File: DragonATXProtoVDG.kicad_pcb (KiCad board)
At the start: 2 copper layers, 159.4 x 85.5 mm, 68 parts, among them IC1 74LS273, IC2 MC6847, IC3 MC14053, J1 Video Output, J2 Board Interconnect Male, J3 JTAG, Q1 MMBT4401, Q2 NPN, Q3 NPN, Q4 NPN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

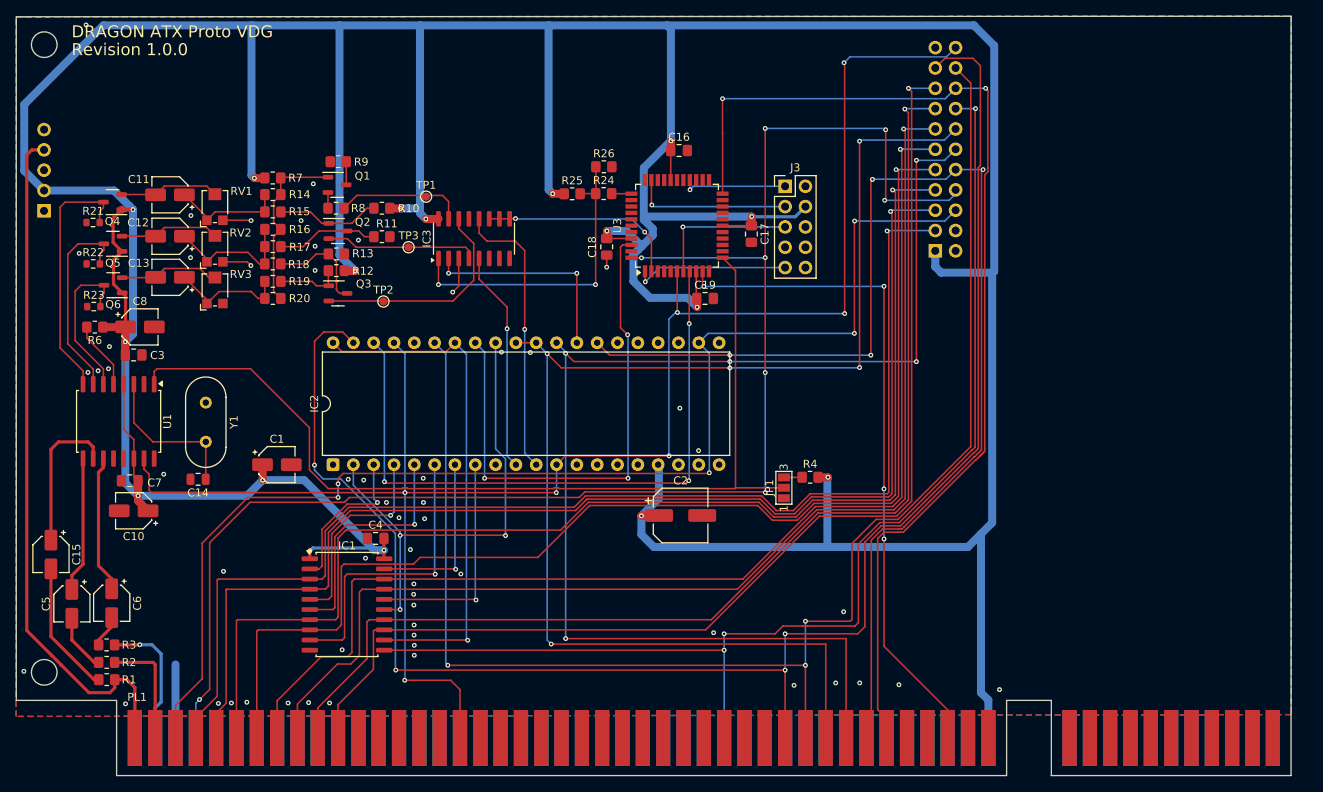
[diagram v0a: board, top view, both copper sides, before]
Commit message: upgrade card edge spec
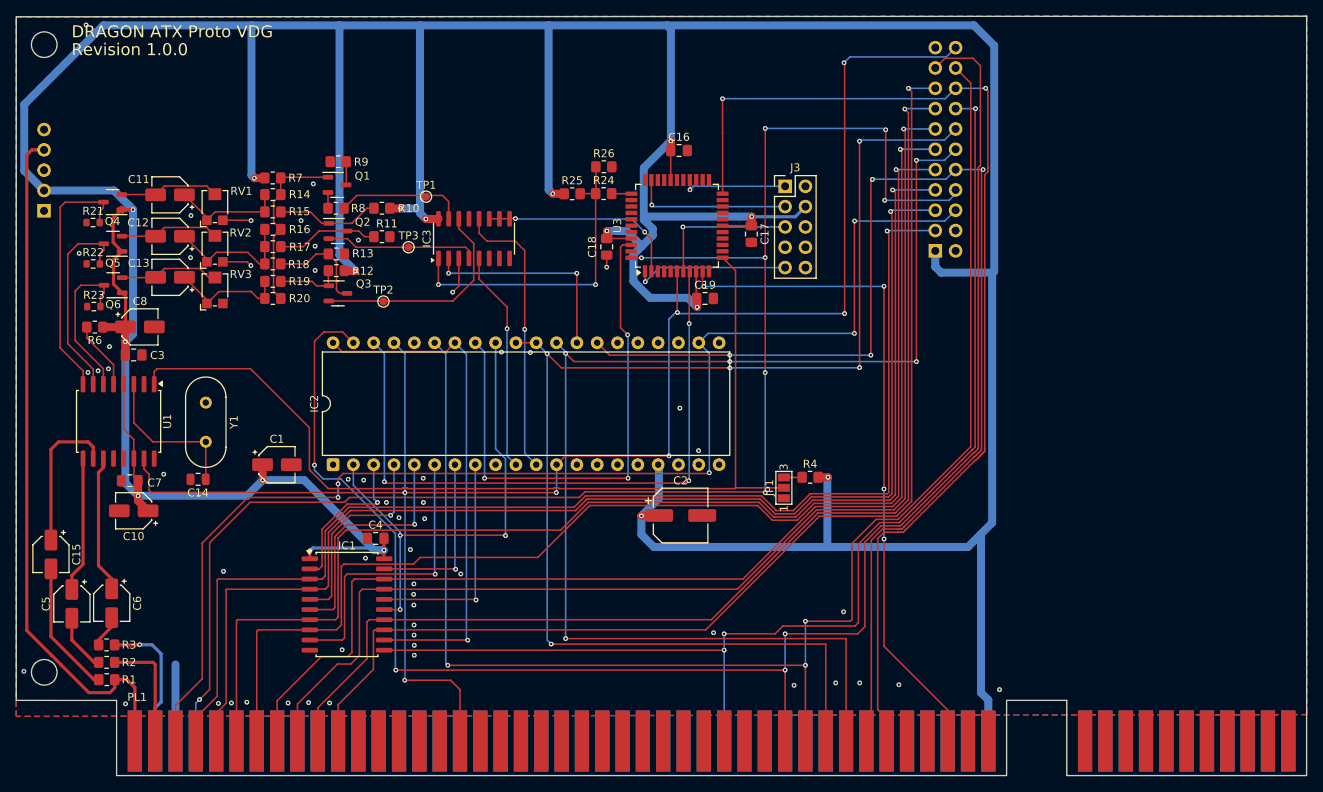
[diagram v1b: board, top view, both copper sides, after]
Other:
- board size 159.4 x 85.5 mm -> 161.3 x 85.5 mm

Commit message: prepare for fabrication
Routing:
- net /HS: track 193.6 -> 180.9 mm, vias 8 -> 6
- net /DL7: track 144.7 -> 143.9 mm, vias 1 -> 0
- net phiB: vias 1 -> 0
- net phiA: vias 1 -> 0
- net GND: vias 56 -> 60

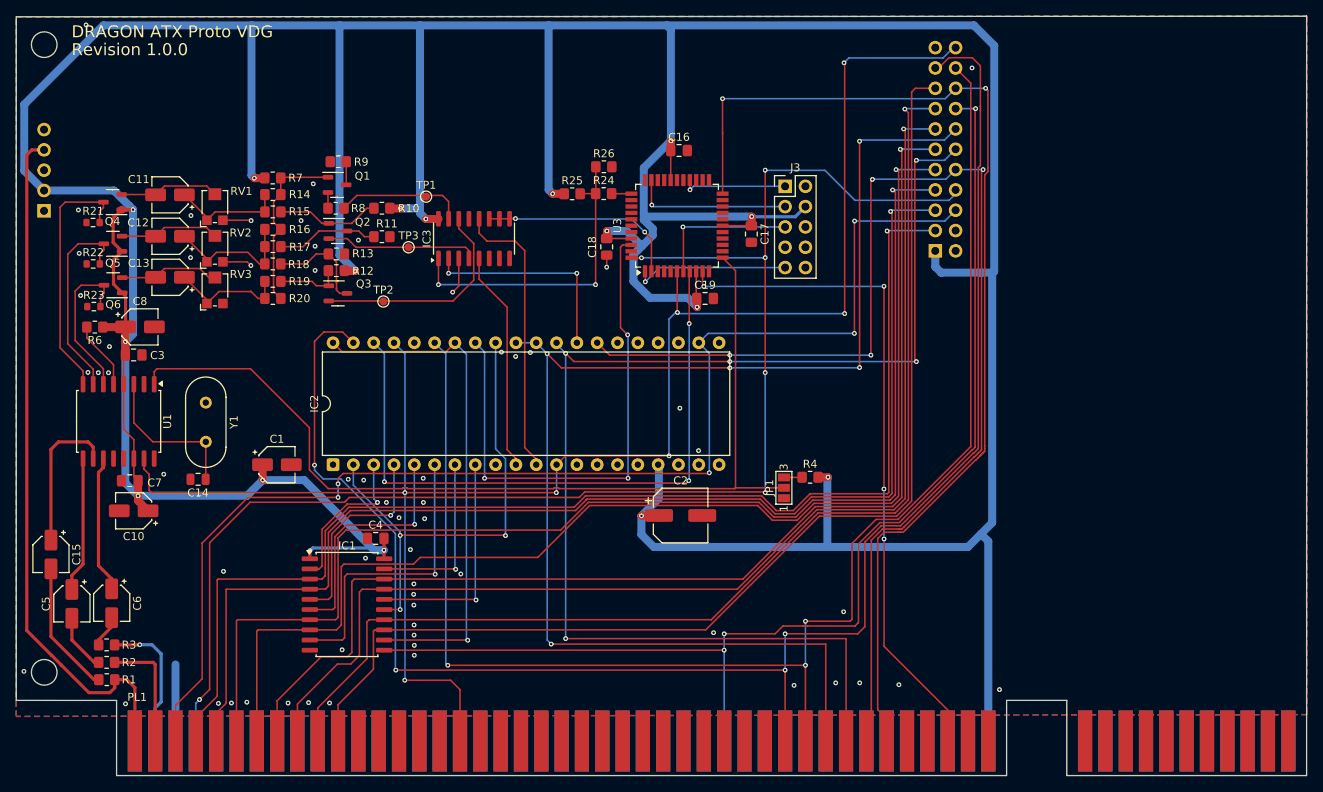
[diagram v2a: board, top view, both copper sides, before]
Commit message: refine design for ATF1504
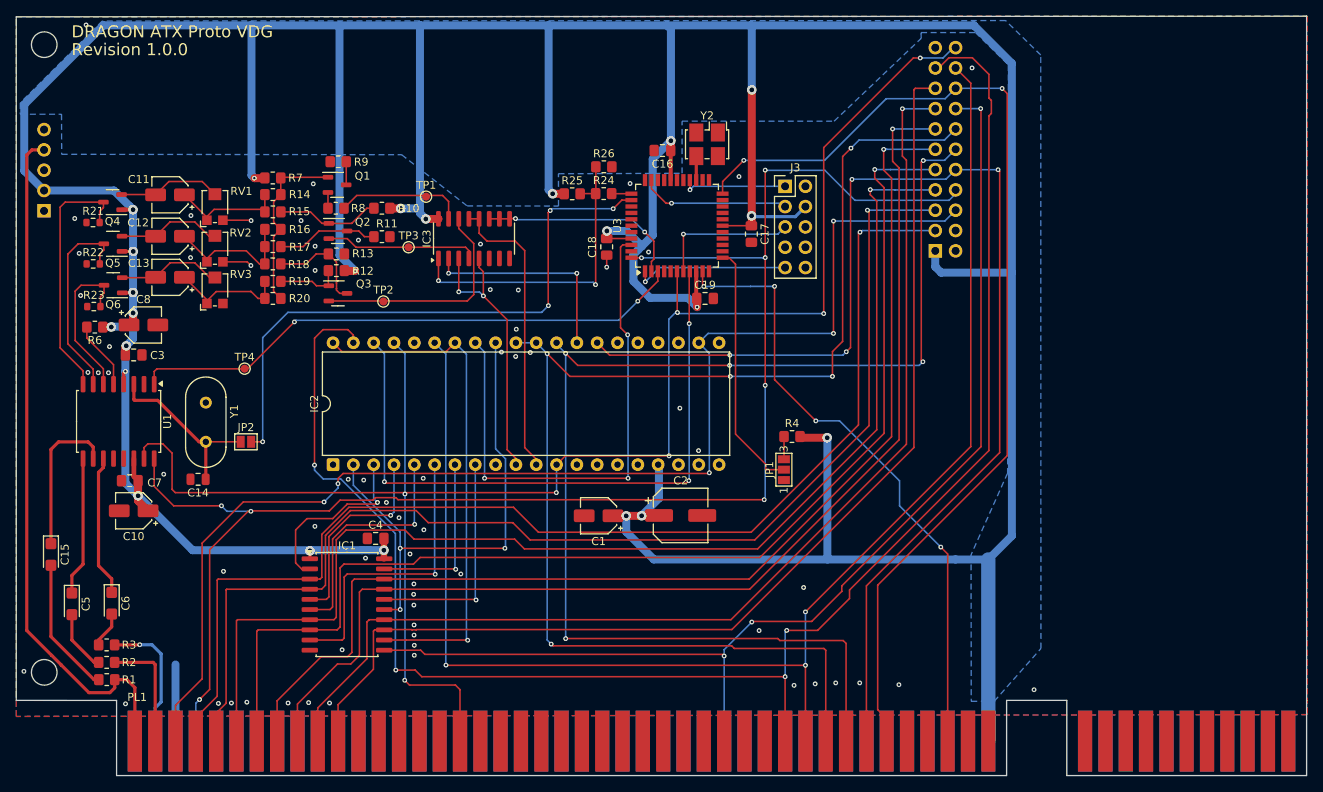
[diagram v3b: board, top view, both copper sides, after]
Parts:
- added JP2: FormatClock, Jumper:SolderJumper-2_P1.3mm_Open_Pad1.0x1.5mm, F.Cu at (92.6, 77.7)
- added TP4: TestPoint_FrameFormat, TestPoint:TestPoint_Pad_D1.0mm, F.Cu at (92.4, 68.6)
- added Y2: 4.433618MHz, Oscillator:Oscillator_SMD_SeikoEpson_SG8002LB-4Pin_5.0x3.2mm_HandSoldering, F.Cu at (150.2, 40.5)
- C15, C5, C6: footprint Capacitor_SMD:CP_Elec_4x5.4 -> Capacitor_Tantalum_SMD:CP_EIA-3216-12_Kemet-S
- U3: value ATF1504ASL-xAx44 -> ATF1502ASL-xAx44
- moved C1 40.7 mm to (136.7, 87.0), turned to 180 degrees
- moved R4 5.57 mm to (160.9, 77.1)
- moved JP1 2.27 mm to (159.8, 81.2)
- moved C16 2.08 mm to (144.7, 41.3), turned to 180 degrees
- moved C8 0.49 mm to (79.8, 63.1)
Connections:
- IC3 pad 13: GND -> phiA
- IC3 pad 3: GND -> phiB
- U1 pad 1: Format -> FrmFormat
- U1 pad 16: ~{NHS} -> /HS
- U3 pad 25: unconnected-(U3-I/O-Pad25) -> PALClock
- U3 pad 3: unconnected-(U3-I/O-Pad3) -> FrmFormat
- U3 pad 30: unconnected-(U3-I/O-Pad30) -> LINE_PULSE
- U3 pad 31: unconnected-(U3-I/O-Pad31) -> SYNC_CONTROL
- U3 pad 33: unconnected-(U3-I/O-Pad33) -> CHROMA_CONTROL
- U3 pad 35: unconnected-(U3-I/O/GCLK3-Pad35) -> FMT_CLOCK
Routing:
- net Format: track 119.4 -> 31.5 mm
- net FMT_CLOCK: track 0.00 -> 74.5 mm, vias 0 -> 4
- net FrmFormat: track 0.00 -> 70.5 mm, vias 0 -> 2
- net /HS: track 180.9 -> 197.8 mm, vias 6 -> 8
- net phiB: track 27.7 -> 35.1 mm, vias 0 -> 2
- net E: track 84.6 -> 78.3 mm
- net /DL3: track 152.7 -> 147.7 mm
- net /RAS: track 147.5 -> 142.8 mm
- net /~{A}/G: track 184.1 -> 179.3 mm
- net GND: track 22.8 -> 18.3 mm, vias 60 -> 67
- net /DL0: track 153.3 -> 148.8 mm
- net /VCLK: track 134.6 -> 130.3 mm
- net /DL6: track 144.3 -> 140.3 mm
- net /DL2: track 154.9 -> 151.1 mm
- net /DL7: track 143.9 -> 140.1 mm
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- added copper zone on B.Cu, net +5V

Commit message: update board render
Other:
- board text added: "JP1 - Format 1-2=PAL 2-3=NTSC JP2 - Clock Source open = direct closed = format controlled"
- board text added: "Revision 1.0.1"
- board text added: "Right pad R14 = Y R15 = B-Y R17 = Y-B R18 = Y-R R19 = R-Y Left Pad R14 & R15 = B-Y+Y R16 & R17 & R18 = Y-B+Y-R+Y R19 & R20 = R-Y+Y"
- board text added: "Test Points TP1 = Luma TP2 = PhiA TP3 = PhiB TP4 = Format Q6/R23 = Red Q5/R22 = Green Q4/R21 = Blue C5 = Chroma C6 = Luma C15 = Composite"
- board text removed: "Revision 1.0.0"
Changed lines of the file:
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@@
 		(layer "User.3")
 	)
-	(gr_text "Revision 1.0.0"
+	(gr_text "Right pad\nR14 = Y\nR15 = B-Y\nR17 = Y-B\nR18 = Y-R\nR19 = R-Y\n\nLeft Pad\nR14 & R15 = B-Y+Y\nR16 & R17 & R18 = Y-B+Y-R+Y\nR19 & R20 = R-Y+Y"
+		(at 194.9958 79.9084 0)
+		(layer "F.SilkS")
+		(effects
+			(font
+				(size 1 1)
+				(thickness 0.1)
+			)
+			(justify left bottom)
+		)
+	)
+	(gr_text "Test Points\n\nTP1 = Luma\nTP2 = PhiA\nTP3 = PhiB\nTP4 = Format\nQ6/R23 = Red\nQ5/R22 = Green\nQ4/R21 = Blue\nC5 = Chroma\nC6 = Luma\nC15 = Composite"
+		(at 194.9958 61.1632 0)
+		(layer "F.SilkS")
+		(effects
+			(font
+				(size 1 1)
+				(thickness 0.1)
+			)
+			(justify left bottom)
+		)
+	)
+	(gr_text "Revision 1.0.1"
 		(at 70.7898 29.5783 0)
 		(layer "F.SilkS")
@@
 			)
 			(justify left bottom)
+		)
+	)
+	(gr_text "JP1 - Format \n   1-2=PAL\n   2-3=NTSC\n\nJP2 - Clock Source\n   open = direct\n   closed = format controlled"
+		(at 194.9958 40.0558 0)
+		(layer "F.SilkS")
+		(effects
+			(font
+				(size 1 1)
+				(thickness 0.1)
+			)
+			(justify left bottom)

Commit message: refresh
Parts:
- removed C11, C12, C13: 10uF, Capacitor_SMD:CP_Elec_4x5.4
- removed Q1: MMBT4401, Library:SOT-23-3
- removed Q2, Q3, Q4, Q5, Q6: NPN, Library:SOT-23-3
- removed R10, R11, R12, R13: 150R, Resistor_SMD:R_0805_2012Metric_Pad1.20x1.40mm_HandSolder
- removed R14: 3K3, Resistor_SMD:R_0805_2012Metric_Pad1.20x1.40mm_HandSolder
- removed R15: 2K2, Resistor_SMD:R_0805_2012Metric_Pad1.20x1.40mm_HandSolder
- removed R16, R20: 2K, Resistor_SMD:R_0805_2012Metric_Pad1.20x1.40mm_HandSolder
- removed R17: 6K8, Resistor_SMD:R_0805_2012Metric_Pad1.20x1.40mm_HandSolder
- removed R18: 4K7, Resistor_SMD:R_0805_2012Metric_Pad1.20x1.40mm_HandSolder
- removed R19: 2K7, Resistor_SMD:R_0805_2012Metric_Pad1.20x1.40mm_HandSolder
- removed R21, R22, R23: 150R, Resistor_SMD:R_0603_1608Metric
- removed R7: 180R, Resistor_SMD:R_0805_2012Metric_Pad1.20x1.40mm_HandSolder
- removed R8: 910R, Resistor_SMD:R_0805_2012Metric_Pad1.20x1.40mm_HandSolder
- removed R9: 100R, Resistor_SMD:R_0805_2012Metric_Pad1.20x1.40mm_HandSolder
- removed RV1, RV2, RV3: 50K, Potentiometer_SMD:Potentiometer_Bourns_TC33X_Vertical
- added C20: 0.1uF, Capacitor_SMD:C_0603_1608Metric_Pad1.08x0.95mm_HandSolder, F.Cu at (92.4, 43.9)
- added C21: 10uF, Capacitor_Tantalum_SMD:CP_EIA-3216-10_Kemet-I_Pad1.58x1.35mm_HandSolder, F.Cu at (93.5, 60.0)
- added C22: 0.1uF, Capacitor_SMD:C_0603_1608Metric_Pad1.08x0.95mm_HandSolder, F.Cu at (92.1, 57.1)
- added C9: 10uF, Capacitor_Tantalum_SMD:CP_EIA-3216-10_Kemet-I_Pad1.58x1.35mm_HandSolder, F.Cu at (92.5, 41.0)
- added R27: 10K, Resistor_SMD:R_0603_1608Metric_Pad0.98x0.95mm_HandSolder, F.Cu at (94.0, 43.9)
- added R5: 2k7, Resistor_SMD:R_0603_1608Metric_Pad0.98x0.95mm_HandSolder, F.Cu at (85.2, 48.2)
- added U2: LMH1251, Package_SO:TSSOP-24_4.4x7.8mm_P0.65mm, F.Cu at (91.7, 51.1)
- moved PL1 0.08 mm to (152.5, 118.0)
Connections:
- IC3 pad 11: LUM CONTROL -> SYNC_CONTROL
- IC3 pad 9: LUM CONTROL -> CHROMA_CONTROL
- Y2 pad 4: GND -> +5V
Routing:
- net ~{HS}: track 82.4 -> 122.2 mm, vias 3 -> 5
- net ~{FS}: track 217.5 -> 257.0 mm, vias 7 -> 9
- net SYNC_CONTROL: track 0.00 -> 31.5 mm
- net CHROMA_CONTROL: track 0.00 -> 25.8 mm
- net +5V: track 637.9 -> 662.7 mm, vias 23 -> 20
- net /~{Y}: track 22.5 -> 0.00 mm
- net RED: track 19.9 -> 42.1 mm
- net GREEN: track 25.3 -> 45.2 mm
- net Net-(C12-Pad1): track 17.4 -> 0.00 mm
- net BLUE: track 31.7 -> 48.7 mm
- net Net-(C13-Pad1): track 15.0 -> 0.00 mm
- net Net-(C11-Pad1): track 14.7 -> 0.00 mm
- net LUM': track 16.2 -> 30.8 mm
- net phiA': track 28.7 -> 41.9 mm
- net Net-(Q6-B): track 13.1 -> 0.00 mm
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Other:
- board size 161.3 x 85.5 mm -> 131.3 x 85.5 mm
- board text added: "Revision 1.1.0"
- board text removed: "Revision 1.0.1"

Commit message: update
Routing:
- net /GM0: track 167.4 -> 169.3 mm, vias 5 -> 4
- net /GM1: track 160.6 -> 162.4 mm, vias 5 -> 4
- net ~{FS}: track 257.0 -> 256.2 mm
- net /Q7: track 64.4 -> 65.0 mm
